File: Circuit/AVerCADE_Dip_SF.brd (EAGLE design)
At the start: 71.1 x 40.6 mm, 37 parts, among them IC1 MEGA8-P, K1 USB-B

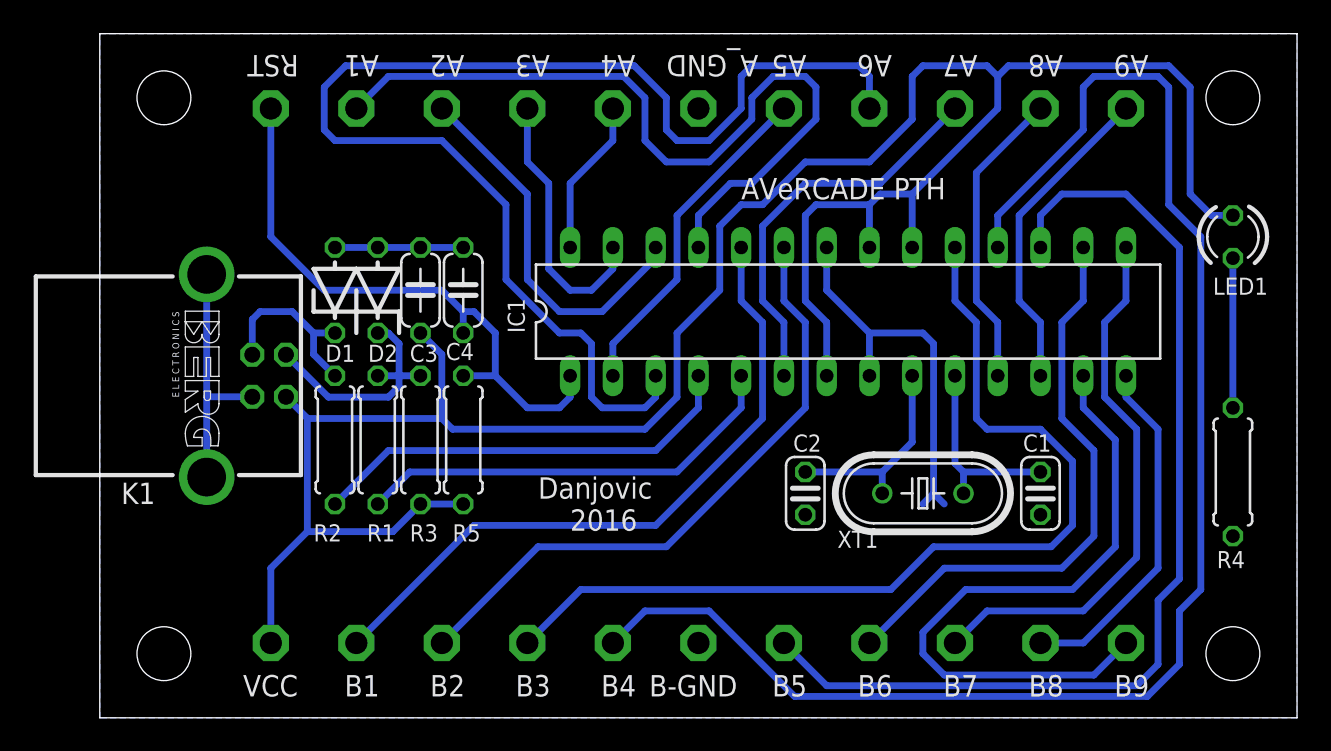
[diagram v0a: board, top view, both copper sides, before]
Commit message: Enhanced PTH board for homemade built.
The component pads have been enlarged to ease the home built versions of the board.
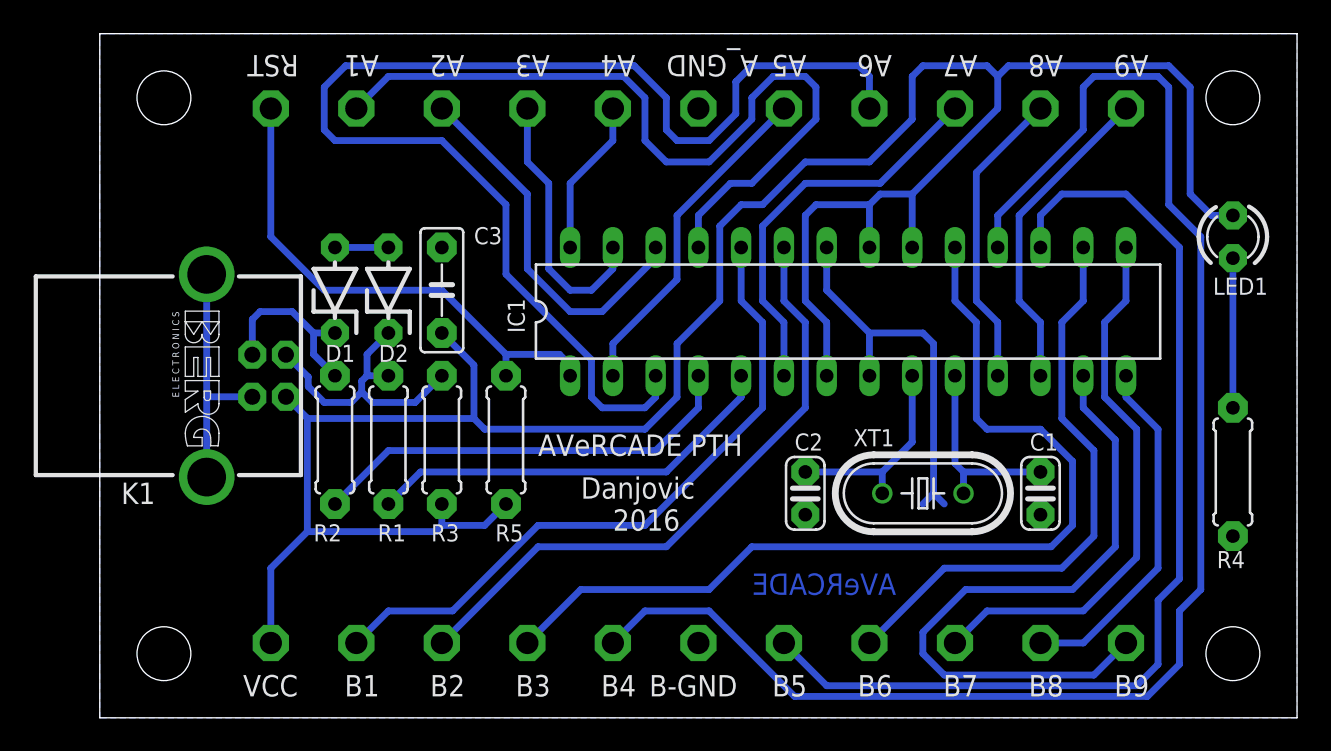
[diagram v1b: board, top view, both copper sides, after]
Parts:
- removed C4: .1u, rcl:C050-024X044
- C1, C2: device rcl:C025-024X044 -> rcl:C025-24X044L
- C3: device rcl:C050-024X044 -> rcl:C050-025X075L
- D1, D2: device diode:ZDIO-5 -> diode:ZDIO-5L
- K1: device con-berg:PN61729-S -> con-berg:PN61729-SL
- LED1: device led:LED3MM -> led:LED3MML
- R1, R2, R3, R4: device rcl:0207/7 -> rcl:0207/7L
- R5: value 4k7 -> 10k; device rcl:0207/7 -> rcl:0207/7L
- moved R5 2.54 mm to (24.1, 16.5)
- moved C3 1.27 mm to (20.3, 25.4)
- moved R3 1.27 mm to (20.3, 16.5)
- moved D2 0.63 mm to (17.1, 25.4)
- moved R1 0.63 mm to (17.1, 16.5)
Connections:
- net D+: now also R2.3; no longer R2.1
- net D-: now also R1.3, R3.4; no longer R1.1, R3.2
- net DM: now also R1.4; no longer R1.2
- net DP: now also R2.4; no longer R2.2
- net GND: now also R4.3; no longer C4.2, R4.1
- net N$11: now also R4.4; no longer R4.2
- net RST: now also R5.4; no longer C4.1, R5.2
- net VCC: now also R3.3, R5.3; no longer R3.1, R5.1
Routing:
- net RST: track 35.8 -> 30.5 mm
- net GND: track 45.8 -> 41.4 mm
- net VCC: track 141.4 -> 145.5 mm
- net D-: track 14.6 -> 17.4 mm
- net DM: track 25.9 -> 24.9 mm
- net N$7: track 76.1 -> 75.3 mm
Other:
- board text added: "AVeRCADE"

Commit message: Added bootloader invoke button, increased clearance on LED pads
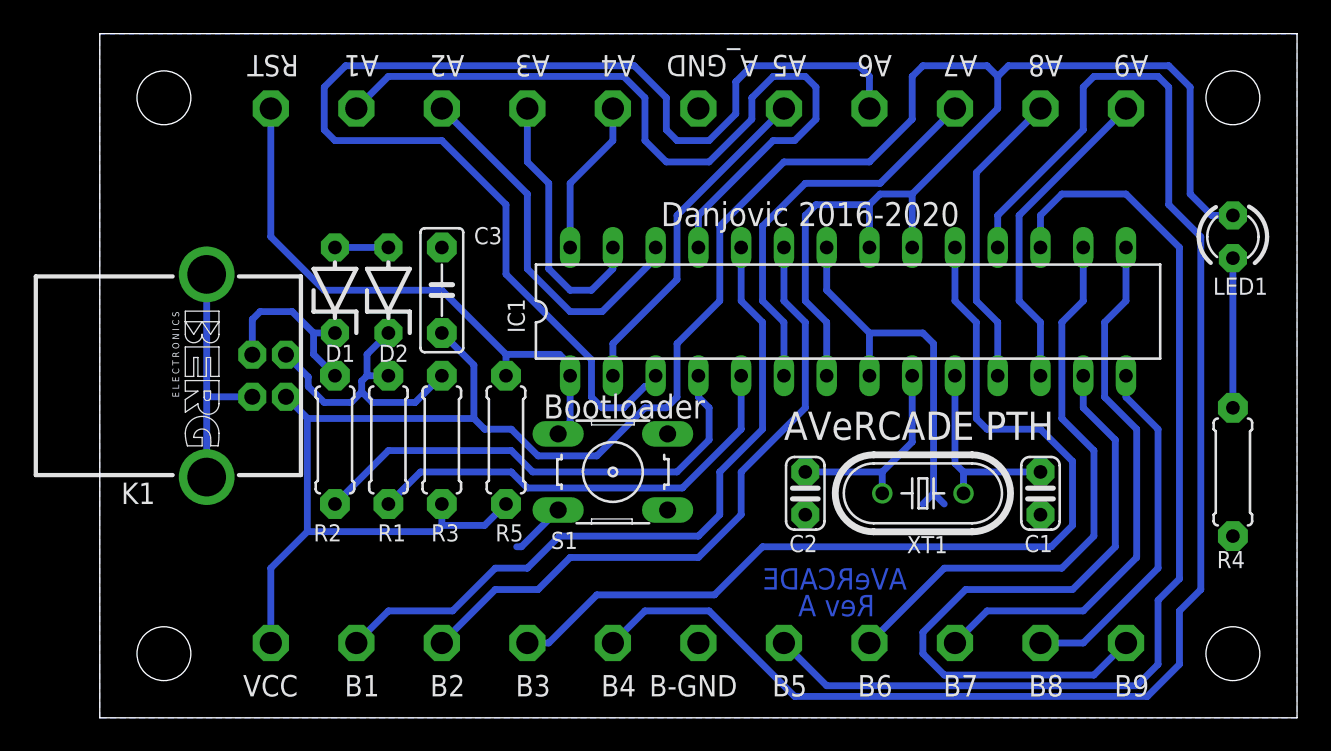
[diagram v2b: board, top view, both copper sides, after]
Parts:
- added S1: (no value), switch-omron:B3F-10XX
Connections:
- net GND: now also S1.3
- net RST: now also S1.1
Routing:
- net RST: track 30.5 -> 34.2 mm
- net GND: track 41.4 -> 44.7 mm
- net DP: track 25.9 -> 28.9 mm
- net N$3: track 40.0 -> 42.2 mm
- net DM: track 24.9 -> 26.8 mm
- net N$4: track 37.4 -> 38.9 mm
- net VCC: track 145.5 -> 146.8 mm
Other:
- board text added: "Bootloader"
- board text added: "Danjovic 2016-2020"
- board text added: "Rev A"
- board text removed: "2016"
- board text removed: "Danjovic"
